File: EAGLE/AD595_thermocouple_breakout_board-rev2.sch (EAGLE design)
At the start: 5 parts

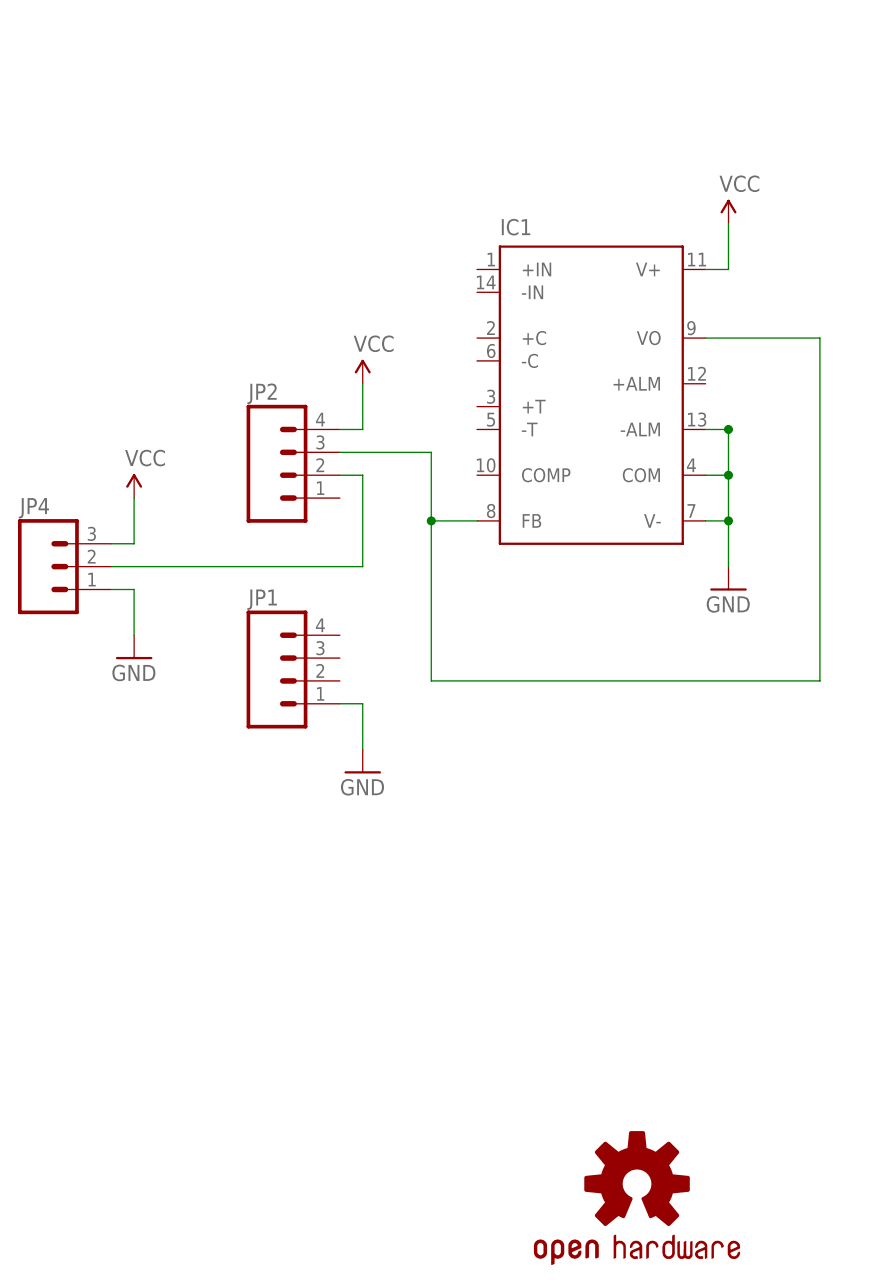
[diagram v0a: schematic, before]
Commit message: Fix done to board, exposed copper for Thermocouple pads. Added an alarm LED and swapped right-angle headers with 3-pin screw terminal for control signal output.
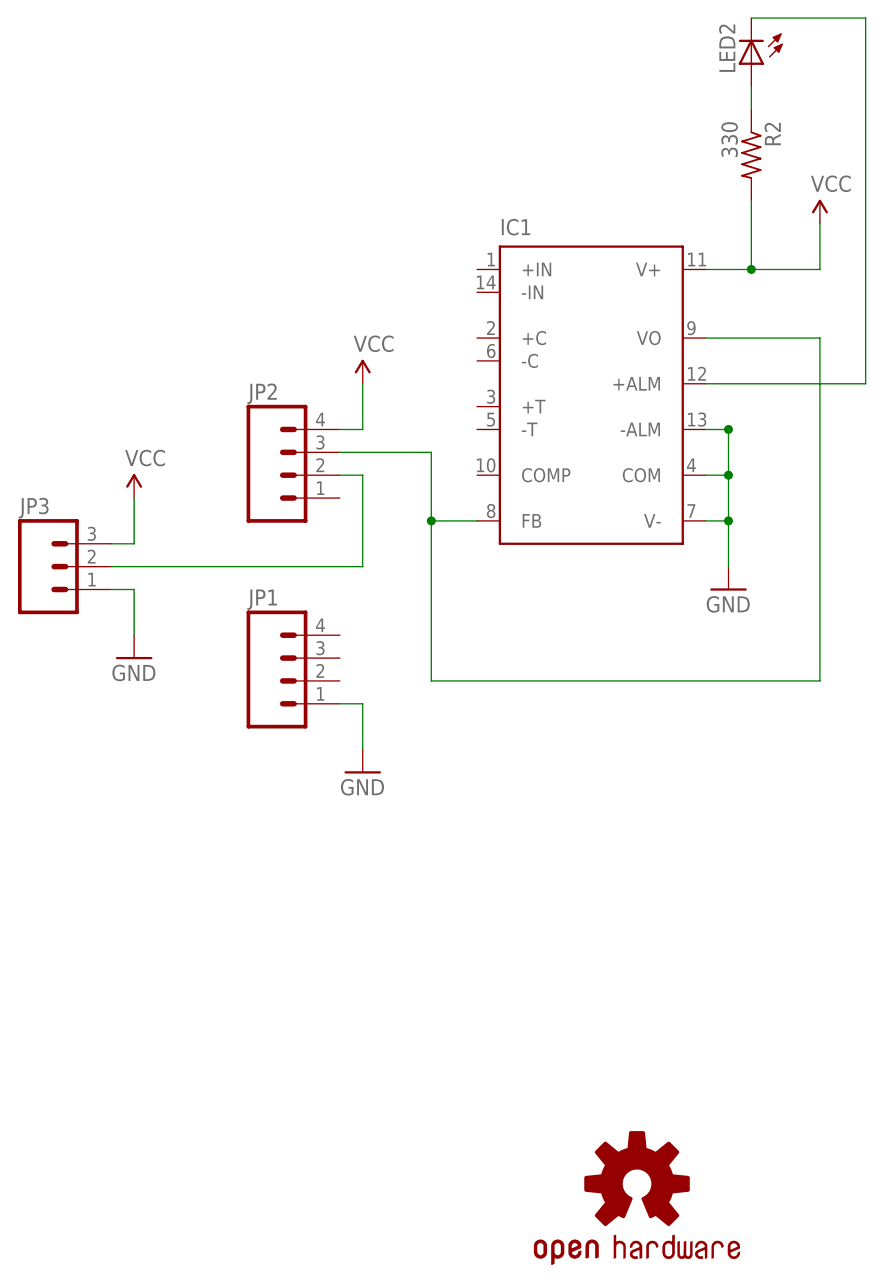
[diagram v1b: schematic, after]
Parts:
- removed JP4: (no value), SparkFun:M03LOCK
- added JP3: (no value), SparkFun-Connectors:M03SCREW_LOCK
- added LED2: (no value), led:LED5MM
- added R2: 330, rcl:R-US_0207/7
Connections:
- new net N$7: LED2.A, R2.1
- new net N$8: IC1.+ALM, LED2.C
- net GND: now also JP3.1; no longer JP4.1
- net N$1: now also JP3.2; no longer JP4.2
- net VCC: now also JP3.3, R2.2; no longer JP4.3
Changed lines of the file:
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@@
 <?xml version="1.0" encoding="utf-8"?>
 <!DOCTYPE eagle SYSTEM "eagle.dtd">
-<eagle version="6.1">
+<eagle version="6.2">
 <drawing>
 <settings>
@@
 <part name="P+1" library="SparkFun" deviceset="VCC" device=""/>
 <part name="P+2" library="SparkFun" deviceset="VCC" device=""/>
-<part name="JP4" library="SparkFun" deviceset="M03" device="LOCK"/>
 <part name="P+3" library="SparkFun" deviceset="VCC" device=""/>
 <part name="GND3" library="SparkFun" deviceset="GND" device=""/>
 <part name="FRAME1" library="SparkFun" deviceset="FRAME-LETTER" device=""/>
 <part name="U$1" library="SparkFun" deviceset="OSHW-LOGO" device="S"/>
+<part name="LED2" library="led" deviceset="LED" device="5MM"/>
+<part name="R2" library="rcl" deviceset="R-US_" device="0207/7" value="330"/>
+<part name="JP3" library="SparkFun-Connectors" deviceset="M03" device="SCREW_LOCK"/>
 </parts>
 <sheets>
@@
 <instance part="GND2" gate="1" x="68.58" y="40.64"/>
 <instance part="P+1" gate="1" x="27.94" y="63.5"/>
-<instance part="P+2" gate="1" x="68.58" y="81.28"/>
-<instance part="JP4" gate="G$1" x="-7.62" y="43.18"/>
+<instance part="P+2" gate="1" x="78.74" y="81.28"/>
 <instance part="P+3" gate="1" x="2.54" y="50.8"/>
 <instance part="GND3" gate="1" x="2.54" y="33.02"/>
@@
 <instance part="FRAME1" gate="G$2" x="78.74" y="-45.72"/>
 <instance part="U$1" gate="G$1" x="58.42" y="-25.4"/>
+<instance part="LED2" gate="G$1" x="71.12" y="99.06" rot="R180"/>
+<instance part="R2" gate="G$1" x="71.12" y="88.9" rot="R270"/>
+<instance part="JP3" gate="G$1" x="-7.62" y="43.18"/>
 </instances>
 <busses>
@@
 <wire x1="0" y1="40.64" x2="2.54" y2="40.64" width="0.1524" layer="91"/>
 <wire x1="2.54" y1="40.64" x2="2.54" y2="35.56" width="0.1524" layer="91"/>
-<pinref part="JP4" gate="G$1" pin="1"/>
 <pinref part="GND3" gate="1" pin="GND"/>
+<pinref part="JP3" gate="G$1" pin="1"/>
 </segment>
 <segment>
@@
 </segment>
 <segment>
-<wire x1="68.58" y1="76.2" x2="68.58" y2="81.28" width="0.1524" layer="91"/>
-<wire x1="66.04" y1="76.2" x2="68.58" y2="76.2" width="0.1524" layer="91"/>
+<wire x1="78.74" y1="76.2" x2="78.74" y2="81.28" width="0.1524" layer="91"/>
+<wire x1="66.04" y1="76.2" x2="71.12" y2="76.2" width="0.1524" layer="91"/>
 <pinref part="IC1" gate="G$1" pin="V+"/>
 <pinref part="P+2" gate="1" pin="VCC"/>
+<wire x1="71.12" y1="76.2" x2="78.74" y2="76.2" width="0.1524" layer="91"/>
+<wire x1="71.12" y1="76.2" x2="71.12" y2="83.82" width="0.1524" layer="91"/>
+<pinref part="R2" gate="G$1" pin="2"/>
+<junction x="71.12" y="76.2"/>
 </segment>
 <segment>
 <wire x1="0" y1="45.72" x2="2.54" y2="45.72" width="0.1524" layer="91"/>
 <wire x1="2.54" y1="45.72" x2="2.54" y2="50.8" width="0.1524" layer="91"/>
-<pinref part="JP4" gate="G$1" pin="3"/>
 <pinref part="P+3" gate="1" pin="VCC"/>
+<pinref part="JP3" gate="G$1" pin="3"/>
 </segment>
 </net>
@@
 <wire x1="27.94" y1="53.34" x2="25.4" y2="53.34" width="0.1524" layer="91"/>
 <pinref part="JP2" gate="G$1" pin="2"/>
-<pinref part="JP4" gate="G$1" pin="2"/>
-</segment>
-</net>
+<pinref part="JP3" gate="G$1" pin="2"/>
+</segment>
+</net>
+<net name="N$7" class="0">
+<segment>
+<wire x1="71.12" y1="93.98" x2="71.12" y2="96.52" width="0.1524" layer="91"/>
+<pinref part="R2" gate="G$1" pin="1"/>
+<pinref part="LED2" gate="G$1" pin="A"/>
+</segment>
+</net>
+<net name="N$8" class="0">
+<segment>
+<wire x1="71.12" y1="104.14" x2="83.82" y2="104.14" width="0.1524" layer="91"/>
+<pinref part="LED2" gate="G$1" pin="C"/>
+<pinref part="IC1" gate="G$1" pin="+ALM"/>
+<wire x1="66.04" y1="63.5" x2="83.82" y2="63.5" width="0.1524" layer="91"/>
+<wire x1="83.82" y1="63.5" x2="83.82" y2="104.14" width="0.1524" layer="91"/>
+</segment>
+</net>
